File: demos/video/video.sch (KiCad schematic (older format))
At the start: 5 parts, among them J4 DB9FEM, P1 BNC, P2 BNC, P3 BNC, P8 BNC

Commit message: Pcbnew: Minor fix in hotkeys. Demos: add an example to use  a local fp-lib-table and local libs, and update schematics and boards.
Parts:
- J4: footprint (none) -> connect:DB9FC
- P1, P2, P3, P8: footprint (none) -> discret:SUBCLICK
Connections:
- wire segments 147 -> 144
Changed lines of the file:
@@
-EESchema Schematic File Version 2  date 18/11/2010 18:50:34
+EESchema Schematic File Version 2
 LIBS:power
 LIBS:device
@@
 LIBS:xilinx
 LIBS:special
-LIBS:microcontrollers
-LIBS:dsp
-LIBS:microchip
 LIBS:analog_switches
 LIBS:motorola
-LIBS:texas
 LIBS:intel
 LIBS:audio
 LIBS:interface
-LIBS:digital-audio
 LIBS:philips
-LIBS:display
 LIBS:cypress
 LIBS:siliconi
-LIBS:opto
-LIBS:atmel
-LIBS:contrib
-LIBS:valves
 LIBS:video-cache
-EELAYER 24  0
+EELAYER 24 0
 EELAYER END
-$Descr A3 16535 11700
+$Descr A3 16535 11693
+encoding utf-8
 Sheet 1 8
 Title "Video"
@@
 	14900 3150 14800 3150
 Wire Wire Line
-	14800 3150 14800 3350
-Wire Wire Line
-	14800 3350 14800 3650
-Wire Wire Line
-	14800 3650 14800 3850
-Wire Wire Line
-	14800 3850 14800 4050
+	14800 3150 14800 4050
 Text Label 14800 1700 0    60   ~ 0
 Y_OUT
@@
 F 0 "#GND01" H 14800 4150 60  0001 C CNN
 F 1 "GND" H 14800 3950 60  0000 C CNN
+F 2 "" H 14800 4050 60  0001 C CNN
+F 3 "" H 14800 4050 60  0001 C CNN
 	1    14800 4050
 	1    0    0    -1
@@
 F 0 "J4" H 15350 4000 70  0000 C CNN
 F 1 "DB9FEM" H 15350 2900 70  0000 C CNN
+F 2 "connect:DB9FC" H 15350 3450 60  0001 C CNN
+F 3 "" H 15350 3450 60  0001 C CNN
 	1    15350 3450
 	1    0    0    1
@@
 F 0 "#GND02" H 15350 2400 60  0001 C CNN
 F 1 "GND" H 15350 2200 60  0000 C CNN
+F 2 "" H 15350 2300 60  0001 C CNN
+F 3 "" H 15350 2300 60  0001 C CNN
 	1    15350 2300
 	1    0    0    -1
@@
 F 0 "P8" H 15360 2220 60  0000 C CNN
 F 1 "BNC" V 15460 2040 40  0000 C CNN
+F 2 "discret:SUBCLICK" H 15350 2100 60  0001 C CNN
+F 3 "" H 15350 2100 60  0001 C CNN
 	1    15350 2100
 	1    0    0    -1
@@
 F 0 "#GND03" H 12100 2200 40  0001 C CNN
 F 1 "GND" H 12100 2130 40  0000 C CNN
+F 2 "" H 12100 2200 60  0001 C CNN
+F 3 "" H 12100 2200 60  0001 C CNN
 	1    12100 2200
 	1    0    0    -1
@@
 F 0 "#GND04" H 12100 3000 40  0001 C CNN
 F 1 "GND" H 12100 2930 40  0000 C CNN
+F 2 "" H 12100 3000 60  0001 C CNN
+F 3 "" H 12100 3000 60  0001 C CNN
 	1    12100 3000
 	1    0    0    -1
@@
 F 0 "#GND05" H 12100 1400 40  0001 C CNN
 F 1 "GND" H 12100 1330 40  0000 C CNN
+F 2 "" H 12100 1400 60  0001 C CNN
+F 3 "" H 12100 1400 60  0001 C CNN
 	1    12100 1400
 	1    0    0    -1
@@
 F 0 "P3" H 12110 2920 60  0000 C CNN
 F 1 "BNC" V 12210 2740 40  0000 C CNN
+F 2 "discret:SUBCLICK" H 12100 2800 60  0001 C CNN
+F 3 "" H 12100 2800 60  0001 C CNN
 	1    12100 2800
 	1    0    0    -1
@@
 F 0 "P2" H 12110 2120 60  0000 C CNN
 F 1 "BNC" V 12210 1940 40  0000 C CNN
+F 2 "discret:SUBCLICK" H 12100 2000 60  0001 C CNN
+F 3 "" H 12100 2000 60  0001 C CNN
 	1    12100 2000
 	1    0    0    -1
@@
 F 0 "P1" H 12110 1320 60  0000 C CNN
 F 1 "BNC" V 12210 1140 40  0000 C CNN
+F 2 "discret:SUBCLICK" H 12100 1200 60  0001 C CNN
+F 3 "" H 12100 1200 60  0001 C CNN
 	1    12100 1200
 	1    0    0    -1

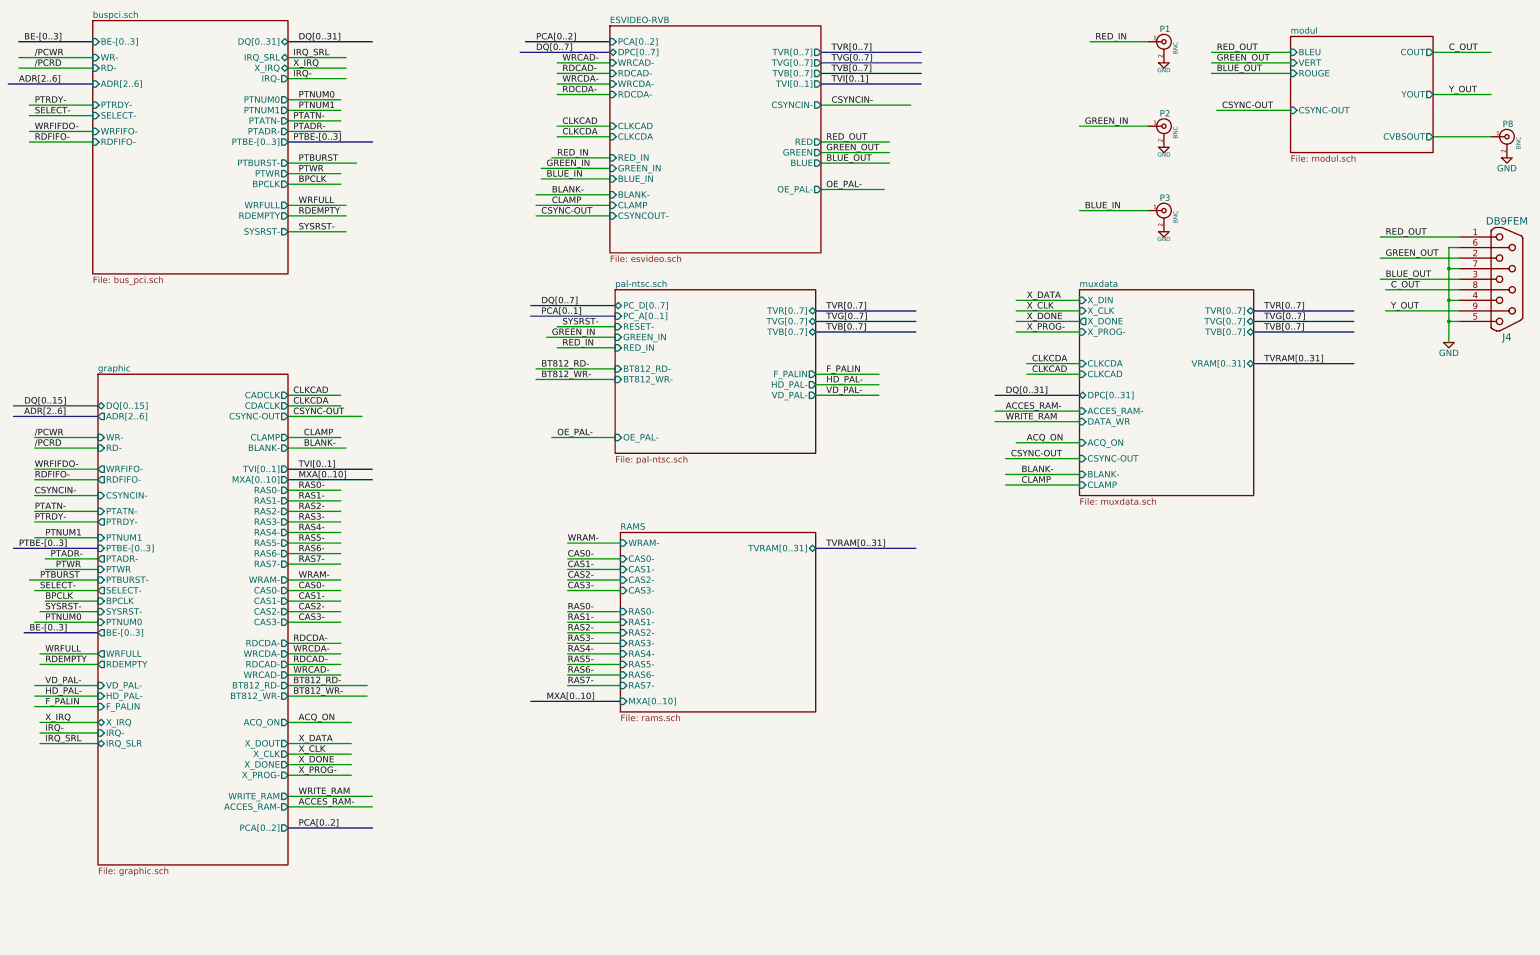
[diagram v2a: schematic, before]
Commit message: demos/ schematic tidying
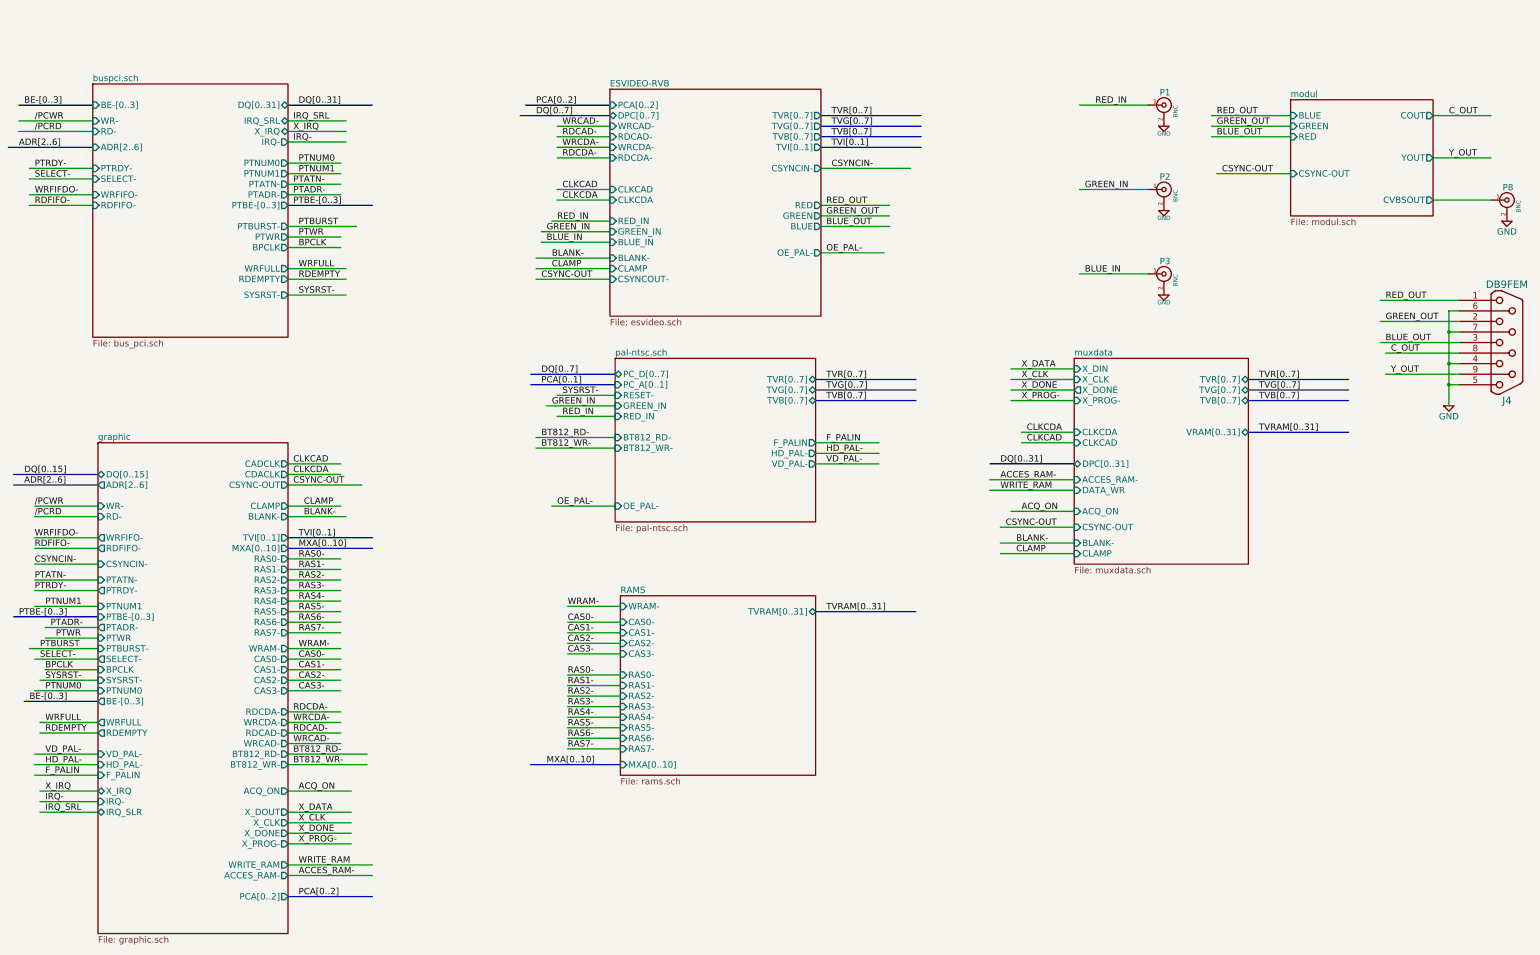
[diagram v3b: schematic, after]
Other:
- moved on the sheet: J4, P1, P2, P3, P8

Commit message: polygons in footprint body: fix incorrect calculation of polygons with clearance or outline thickness (fix bug #1511366) Clean demos
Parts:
- J4: footprint connect:DB9FC -> Connect:DB9FC
- P1, P2, P3, P8: footprint discret:SUBCLICK -> Discret:SUBCLICK
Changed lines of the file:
@@
 EESchema Schematic File Version 2
+LIBS:video_schlib
 LIBS:power
-LIBS:device
-LIBS:transistors
-LIBS:conn
-LIBS:linear
-LIBS:regul
-LIBS:74xx
-LIBS:cmos4000
-LIBS:adc-dac
-LIBS:memory
-LIBS:xilinx
-LIBS:special
-LIBS:analog_switches
-LIBS:motorola
-LIBS:intel
-LIBS:audio
-LIBS:interface
-LIBS:philips
-LIBS:cypress
-LIBS:siliconi
 LIBS:video-cache
 EELAYER 25 0
@@
 F 0 "J4" H 15350 4600 70  0000 C CNN
 F 1 "DB9FEM" H 15350 3500 70  0000 C CNN
-F 2 "connect:DB9FC" H 15350 4050 60  0001 C CNN
+F 2 "Connect:DB9FC" H 15350 4050 60  0001 C CNN
 F 3 "" H 15350 4050 60  0001 C CNN
 	1    15350 4050
@@
 F 0 "P8" H 15360 2820 60  0000 C CNN
 F 1 "BNC" V 15460 2640 40  0000 C CNN
-F 2 "discret:SUBCLICK" H 15350 2700 60  0001 C CNN
+F 2 "Discret:SUBCLICK" H 15350 2700 60  0001 C CNN
 F 3 "" H 15350 2700 60  0001 C CNN
 	1    15350 2700
@@
 F 0 "P3" H 12110 3520 60  0000 C CNN
 F 1 "BNC" V 12210 3340 40  0000 C CNN
-F 2 "discret:SUBCLICK" H 12100 3400 60  0001 C CNN
+F 2 "Discret:SUBCLICK" H 12100 3400 60  0001 C CNN
 F 3 "" H 12100 3400 60  0001 C CNN
 	1    12100 3400
@@
 F 0 "P2" H 12110 2720 60  0000 C CNN
 F 1 "BNC" V 12210 2540 40  0000 C CNN
-F 2 "discret:SUBCLICK" H 12100 2600 60  0001 C CNN
+F 2 "Discret:SUBCLICK" H 12100 2600 60  0001 C CNN
 F 3 "" H 12100 2600 60  0001 C CNN
 	1    12100 2600
@@
 F 0 "P1" H 12110 1920 60  0000 C CNN
 F 1 "BNC" V 12210 1740 40  0000 C CNN
-F 2 "discret:SUBCLICK" H 12100 1800 60  0001 C CNN
+F 2 "Discret:SUBCLICK" H 12100 1800 60  0001 C CNN
 F 3 "" H 12100 1800 60  0001 C CNN
 	1    12100 1800

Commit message: merge from production git:e53c3af 21.04.2017
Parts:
- J4: footprint Connect:DB9FC -> Connectors:DB9FC
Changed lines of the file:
@@
 LIBS:power
 LIBS:video-cache
-EELAYER 25 0
+EELAYER 26 0
 EELAYER END
 $Descr A3 16535 11693
@@
 F 0 "J4" H 15350 4600 70  0000 C CNN
 F 1 "DB9FEM" H 15350 3500 70  0000 C CNN
-F 2 "Connect:DB9FC" H 15350 4050 60  0001 C CNN
+F 2 "Connectors:DB9FC" H 15350 4050 60  0001 C CNN
 F 3 "" H 15350 4050 60  0001 C CNN
 	1    15350 4050
